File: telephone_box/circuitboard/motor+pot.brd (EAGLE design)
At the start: 39.2 x 33.3 mm, 10 parts, among them J2 TERM-1X02-FABLAB, J3 JACK-2.1MM

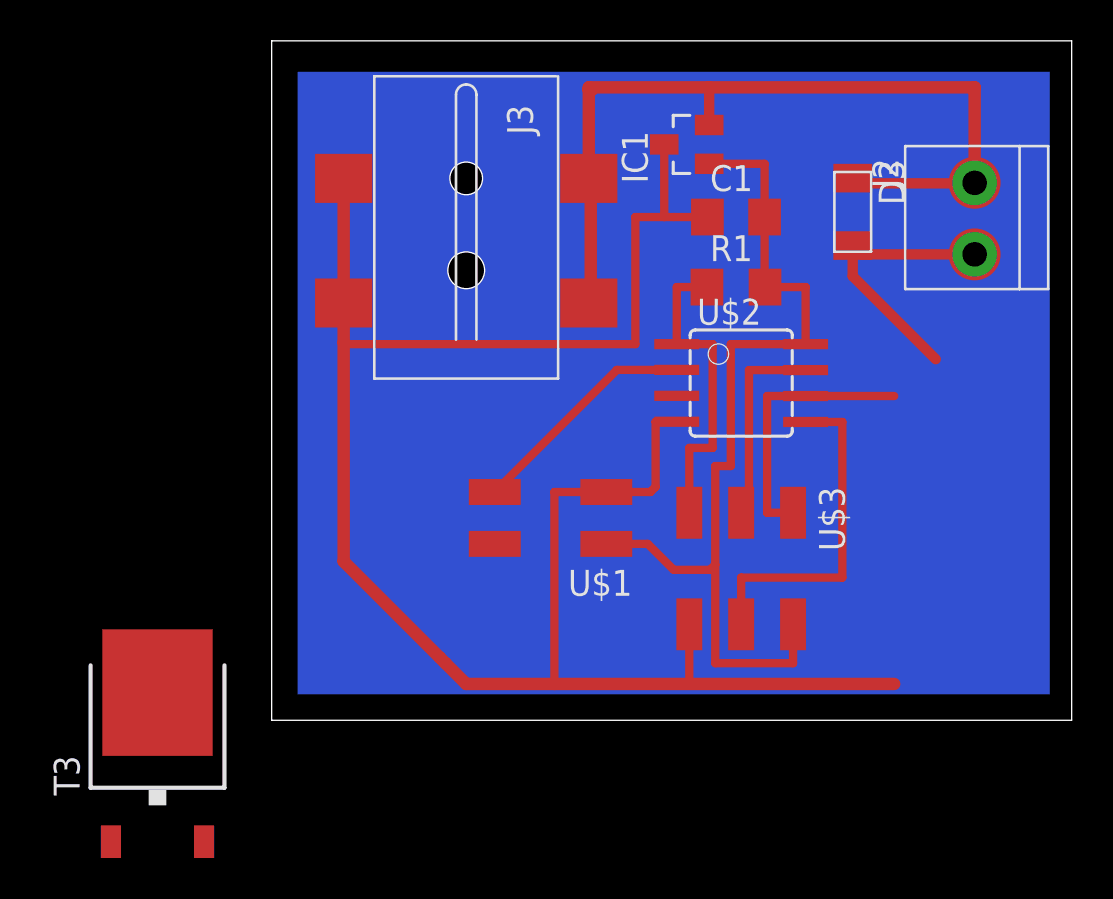
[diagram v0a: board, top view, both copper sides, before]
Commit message: moved stepper out and edited telophone
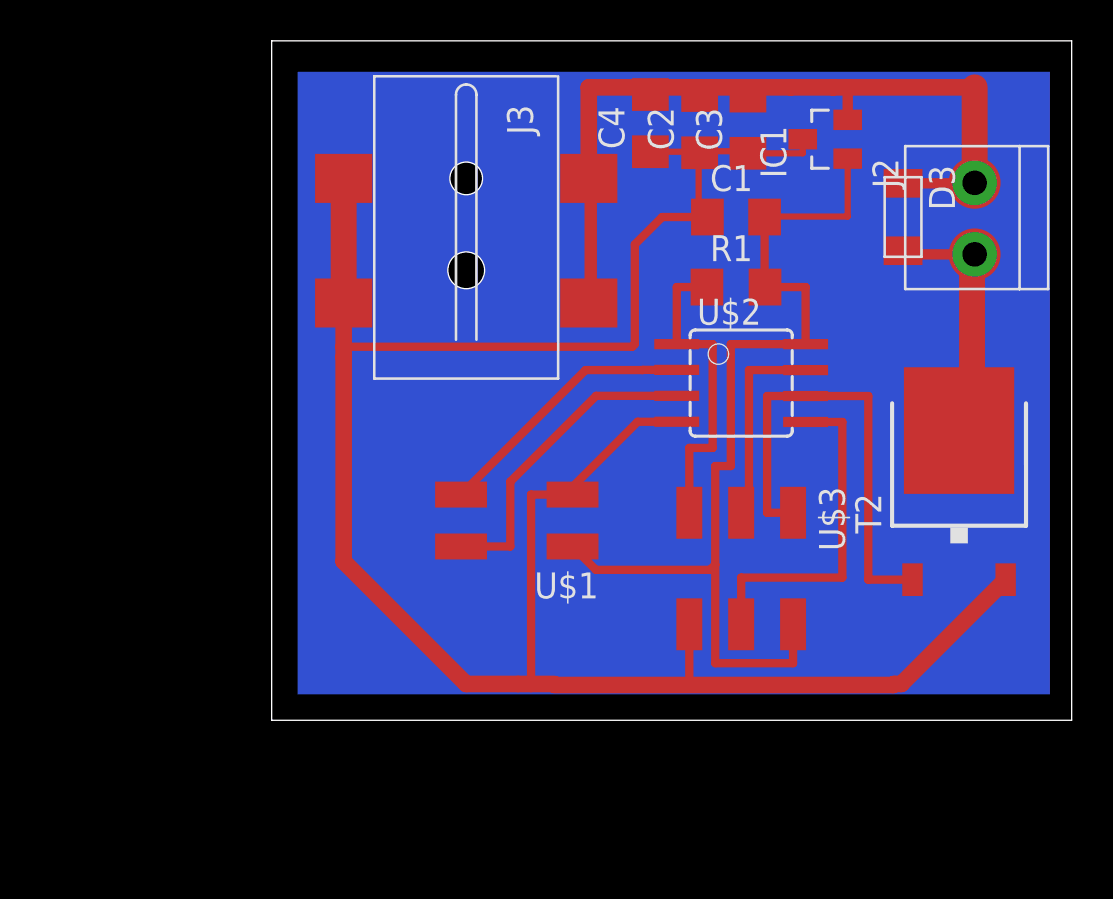
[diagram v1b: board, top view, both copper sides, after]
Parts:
- removed T3: (no value), fab:TO252
- added C2, C3, C4: (no value), fab:C1206
- added T2: (no value), fab:TO252
- moved IC1 6.79 mm to (27.1, 28.4)
- moved D3 2.48 mm to (30.9, 24.6)
- moved U$1 1.66 mm to (12.2, 9.78)
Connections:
- removed net N$2: D3.ANODE, J2.2, T3.2
- new net N$10: D3.ANODE, J2.2, T2.3
- new net PB4: U$1.2, U$2.3
- net GND: now also C2.1, C3.1, C4.1, T2.2; no longer T3.3
- net T1G: now also T2.1; no longer T3.1
- net VIN: now also C2.2, C3.2, C4.2
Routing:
- net PB4: track 0.00 -> 15.5 mm
- net GND: track 97.5 -> 112.0 mm
- net N$2: track 13.4 -> 0.00 mm
- net N$10: track 0.00 -> 12.5 mm
- net T1G: track 13.2 -> 23.5 mm
- net VCC: track 45.3 -> 48.5 mm
- net VIN: track 43.2 -> 40.6 mm
- net POT_IN: track 11.4 -> 13.1 mm
